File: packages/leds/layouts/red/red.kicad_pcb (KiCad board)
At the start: 2 copper layers, 2 parts, among them U1 2V

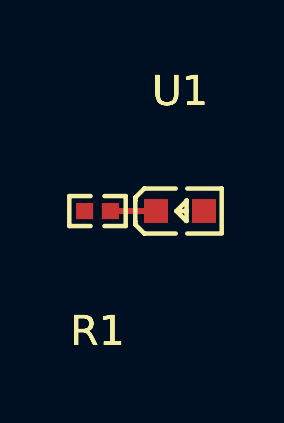
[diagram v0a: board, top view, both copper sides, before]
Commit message: rebuild all packages & regenerate images of changed layouts (silk)
Add new scripts for version bump and build (based on atopile/packages)
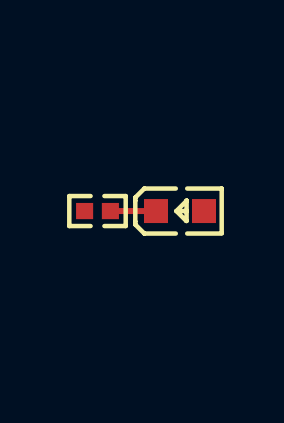
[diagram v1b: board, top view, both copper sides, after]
